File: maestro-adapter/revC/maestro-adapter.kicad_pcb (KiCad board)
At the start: 2 copper layers, 35.6 x 73.7 mm, 49 parts, among them P1 CONN_01X07, P10 CONN_01X03, P11 CONN_01X03, P12 CONN_01X03, P13 CONN_01X03, P14 CONN_01X06, P15 CONN_01X06, P16 CONN_01X03, P2 CONN_01X03, P3 CONN_01X03, P4 CONN_01X03, P5 CONN_01X03, P6 CONN_01X03, P7 CONN_01X03, P8 CONN_01X03, P9 CONN_01X03, U1 Si866x, U2 Si866x

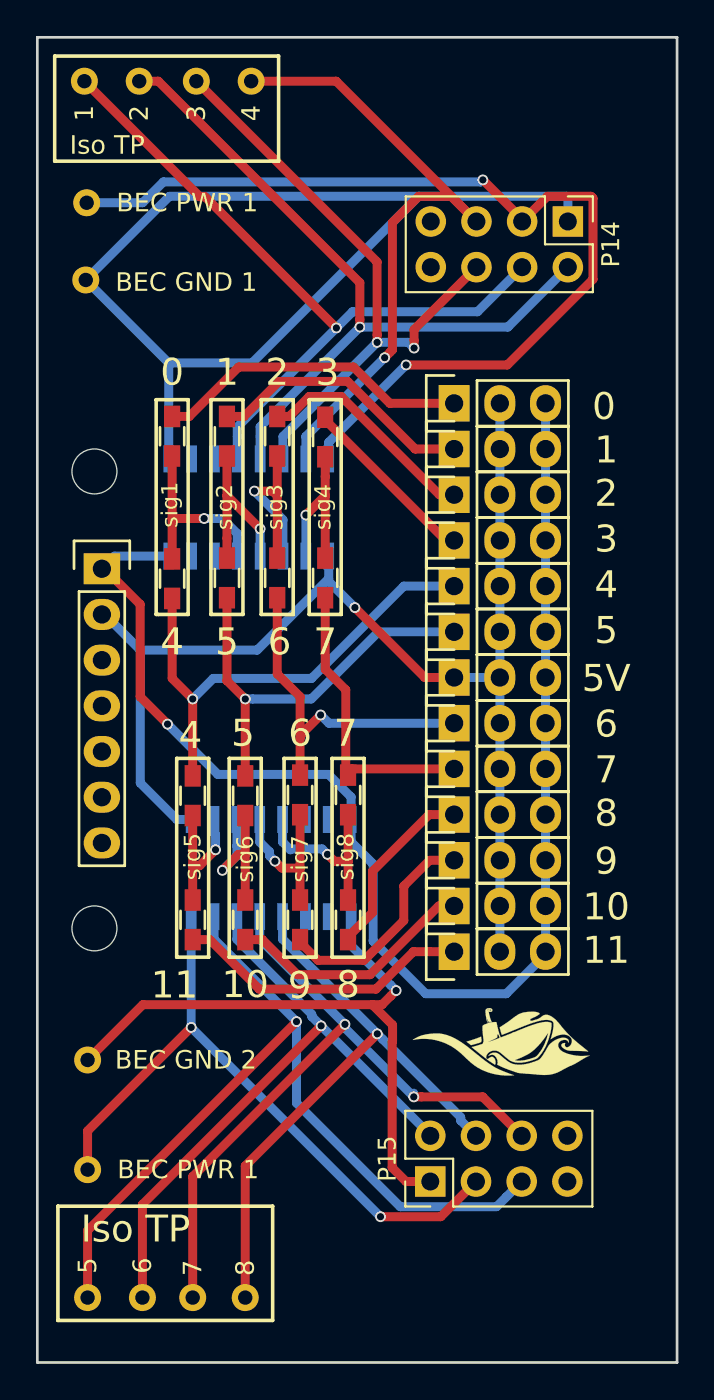
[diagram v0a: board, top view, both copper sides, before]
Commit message: Rerouted the PCB for the smaller pitch connector. The DRC rules checked out.
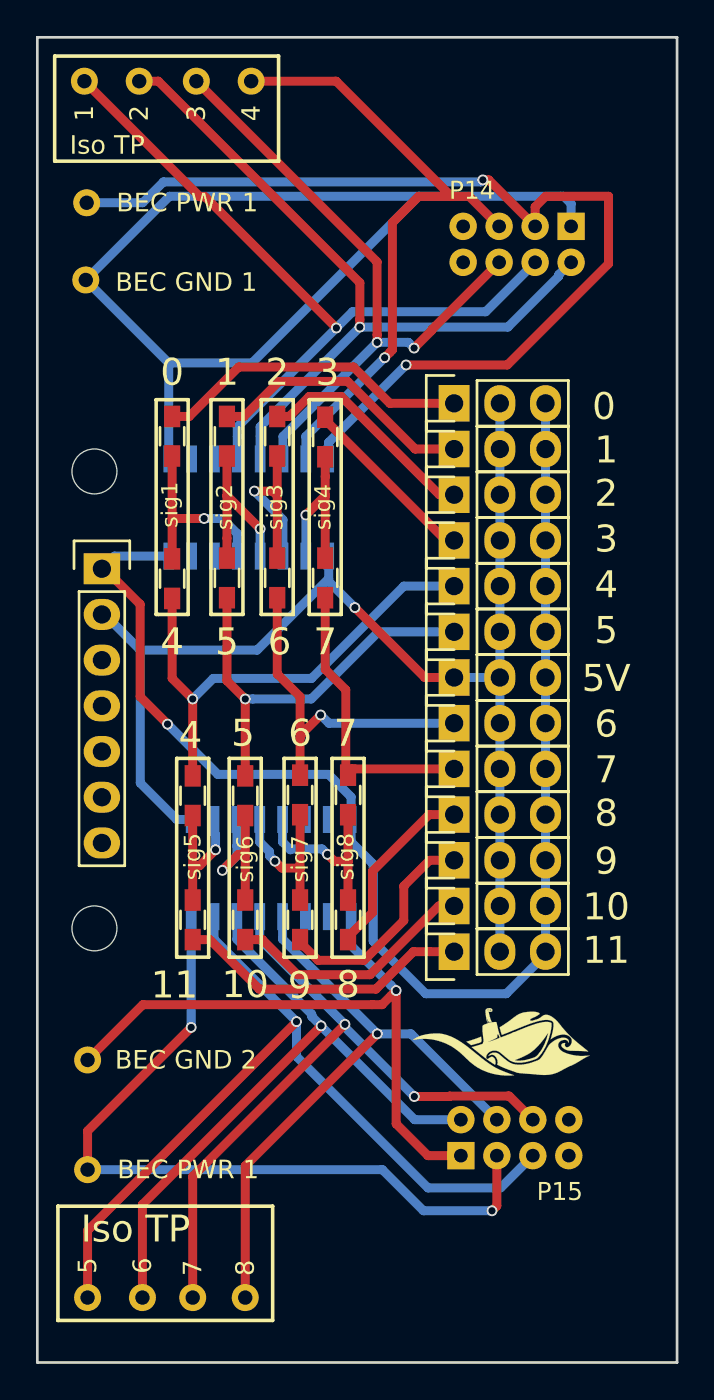
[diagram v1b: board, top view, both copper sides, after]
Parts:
- P14, P15: footprint Pin_Headers:Pin_Header_Straight_2x04_Pitch2.54mm -> MaestroJSTConnector:JST_PUD
- moved P15 5.29 mm to (176.5, 123.2), turned to 0 degrees
- moved P14 3.09 mm to (176.7, 73.5), turned to 180 degrees
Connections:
- P1 pad 3: (no net) -> Net-(P1-Pad3)
- P1 pad 4: (no net) -> Net-(P1-Pad4)
- P1 pad 5: (no net) -> Net-(P1-Pad5)
- P1 pad 6: (no net) -> Net-(P1-Pad6)
- P1 pad 7: (no net) -> Net-(P1-Pad7)
- U1 pad 10: (no net) -> Net-(U1-Pad10)
- U1 pad 11: (no net) -> Net-(U1-Pad11)
- U1 pad 6: (no net) -> Net-(U1-Pad6)
- U1 pad 7: (no net) -> Net-(U1-Pad7)
- U2 pad 10: (no net) -> Net-(U2-Pad10)
- U2 pad 11: (no net) -> Net-(U2-Pad11)
- U2 pad 6: (no net) -> Net-(U2-Pad6)
- U2 pad 7: (no net) -> Net-(U2-Pad7)
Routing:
- net /bec_esc_2: track 37.4 -> 43.6 mm
- net /bec_esc_1: track 54.2 -> 56.3 mm
- net /sig6_isolated: track 35.9 -> 37.2 mm
- net /sig5_isolated: track 47.9 -> 46.7 mm
- net /sig1_isolated: track 41.0 -> 41.8 mm
- net /sig3_isolated: track 35.4 -> 36.2 mm
- net /sig4_isolated: track 36.7 -> 36.1 mm

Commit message: Generated Gerbers to check final layout. Added name to PCB.
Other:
- board text added: "Maestro Adapter Ben Songras May '18 - RevC"
- board text removed: "Maestro Adapter Ryan Summers RS17 - RevB"
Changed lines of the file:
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@@
     (visible_elements FFFEFF7F)
     (pcbplotparams
-      (layerselection 0x00030_80000001)
+      (layerselection 0x010f0_80000001)
       (usegerberextensions false)
       (excludeedgelayer true)
@@
       (outputformat 1)
       (mirror false)
-      (drillshape 1)
+      (drillshape 0)
       (scaleselection 1)
-      (outputdirectory ""))
+      (outputdirectory Gerbers/))
   )
   (net 0 "")
@@
     (effects (font (size 1.03 1.03) (thickness 0.1984)))
   )
-  (gr_text "Maestro Adapter\nRyan Summers\nRS17 - RevB" (at 183.4007 66.4718) (layer B.SilkS)
+  (gr_text "Maestro Adapter\nBen Songras\nMay '18 - RevC" (at 183.4007 66.4718) (layer B.SilkS)
     (effects (font (size 1.5 1.5) (thickness 0.3)) (justify left mirror))
   )
